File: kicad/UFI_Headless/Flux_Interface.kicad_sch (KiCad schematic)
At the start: 55 parts, among them Q10 BSS138DW, Q11 BSS138DW, Q5 2N7002, Q6 BSS138DW, Q7 BSS138DW, Q8 BSS138DW, Q9 BSS138DW, U14 74LVC1G32, U22 TS5A3166DBVR, U30 74LVC2G32, U31 74LVC1G02, U8 74LVC14AD

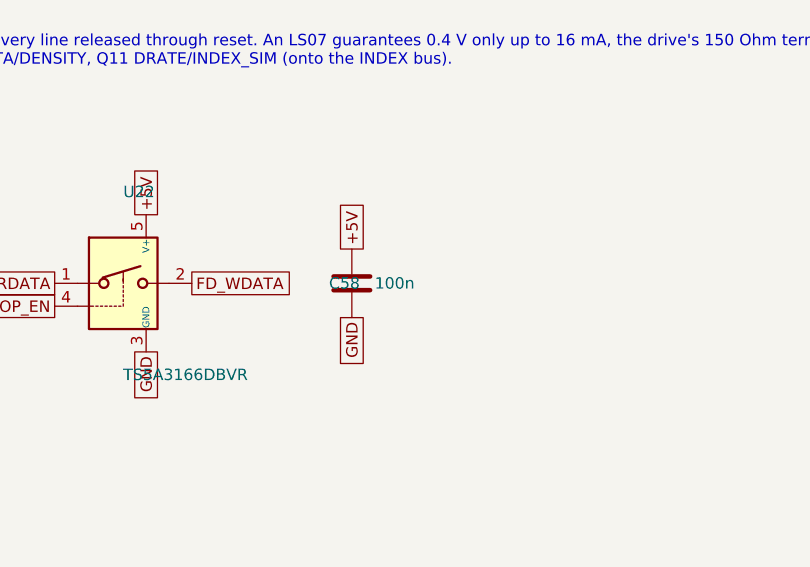
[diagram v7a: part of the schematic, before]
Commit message: KiCad v0.7 rework, stage C part 1 (BOM completion before the release, review note H12): every BOM row now carries an LCSC number, checked against the JLCPCB SMT catalogue on 2026-10-25 (stock in brackets). LAN sheet: U23 W5500 C32843 (9019), J22 HR911105A C12074 (72229, THT), Y2 25 MHz 12 pF +-10 ppm YXC X322525MOB4SI C9006 (basic; load capacitance 12 pF verified on the LCSC parameter page, fits the 18 pF C59/C60), C59/C60 18 pF C0G Yageo CC0603JRNPO9BN180 C107040, C61/C74 10 nF FH 0603B103K500NT C57112 (basic), C71 22 nF Samsung CL10B223KB8NNNC C21122 (basic), C72/C73 6.8 nF FH 0603B682K500NT C1631 (basic), C62 4.7 uF C1779, C63/C69 10 uF C15850, C64-C68/C70 100 nF C14663, FB2 C1002, R109 1M C22935, R111 12.4k 1 % C22865, R112/R113 49.9R 1 % C23185 (basic), R114 10R 1 % C22859 (basic), R115/R116 82R 1 % C23255, R117/R118 330R C23138, R119-R124 10k C25804. Other sheets: R75-R99/R105/R128 1k C21190, R74/R107/R108 10k C25804, R101-R104/R130 470R C23179, R106/R131 100k C25803, C58 100 nF C14663 (value text 100n -> 100nF so it groups with the other 100 nF), D18-D26/D28/D29 PESD3V3L1BA C51450 (48710) like D32-D34, Q5 2N7002 C8545 (basic), U22 TS5A3166DBVR C353035 (10678), J2 DC-005 2.0 C16214 (92305; same pin pattern as the KiCad BarrelJack_Horizontal footprint, placement to be checked in the JLC viewer), J7 2x12 IDC ZHOURI DC3-2.54-24PAS C5144580 (stock 81 - hand soldering stays the recommendation in docs/Bestellung_JLC.md), J12 2x8 IDC DC3-2.54-16PAS C2977594 (4335), J16 2x5 pin header XFCN PZ254V-12-10P C492422 (105667), J21 2x10 pin header PZ254V-12-20P C492427 (63622). Solder jumpers JP5-JP8 are excluded from the BOM (in_bom no) like JP1/JP3 - bare copper, nothing to place. Stock of the review's watch list: U9 SN74LS07DR C371970 4776, D31 ESDA6V1-5SC6 C6650 3010, L1 SRN6045TA-150M C1330797 1866. BOM export (kicad-cli sch export bom, grouped by value/footprint/LCSC): 99 rows, 0 without LCSC, 0 DNP. ERC over the whole project 0 errors / 0 warnings (build/erc.rpt). No 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
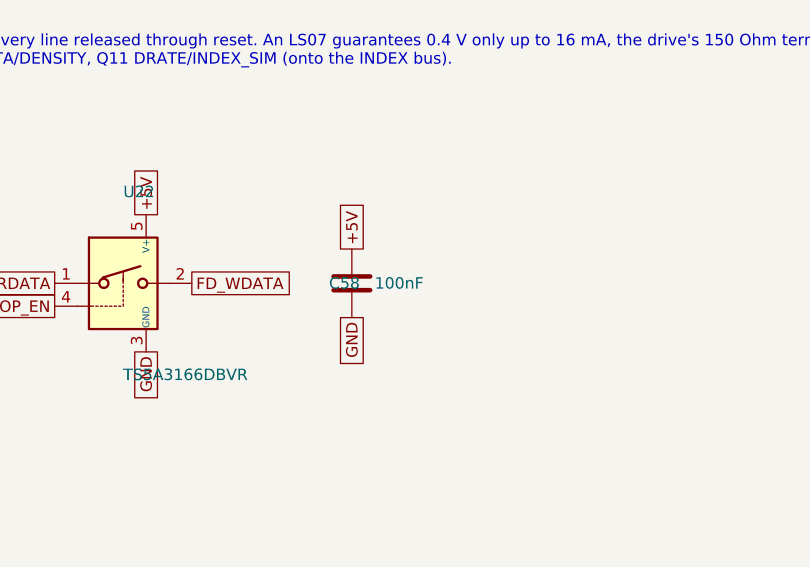
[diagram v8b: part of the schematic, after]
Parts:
- C58: value 100n -> 100nF; LCSC (none) -> C14663
- Q5: LCSC (none) -> C8545
- R106, R131: LCSC (none) -> C25803
- R75, R76, R77, R78, R79, R80, R81, R82, R83, R84, R85, R86, R87, R88, R89, R90, R91: LCSC (none) -> C21190
- U22: LCSC (none) -> C353035
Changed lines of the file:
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@@
+			)
+		)
+		(property "LCSC" "C21190"
+			(at 163.322 250.19 90)
+			(effects
+				(font
+					(size 1.27 1.27)
+				)
+				(hide yes)
 			)
 		)
@@
 			)
 		)
+		(property "LCSC" "C21190"
+			(at 165.862 250.19 90)
+			(effects
+				(font
+					(size 1.27 1.27)
+				)
+				(hide yes)
+			)
+		)
 		(property "Footprint" "Resistor_SMD:R_0603_1608Metric"
 			(at 165.862 250.19 90)
@@
 			)
 		)
+		(property "LCSC" "C21190"
+			(at 168.402 250.19 90)
+			(effects
+				(font
+					(size 1.27 1.27)
+				)
+				(hide yes)
+			)
+		)
 		(property "Footprint" "Resistor_SMD:R_0603_1608Metric"
 			(at 168.402 250.19 90)
@@
 			)
 		)
+		(property "LCSC" "C21190"
+			(at 170.942 250.19 90)
+			(effects
+				(font
+					(size 1.27 1.27)
+				)
+				(hide yes)
+			)
+		)
 		(property "Footprint" "Resistor_SMD:R_0603_1608Metric"
 			(at 170.942 250.19 90)
@@
 			)
 		)
+		(property "LCSC" "C21190"
+			(at 183.642 250.19 90)
+			(effects
+				(font
+					(size 1.27 1.27)
+				)
+				(hide yes)
+			)
+		)
 		(property "Footprint" "Resistor_SMD:R_0603_1608Metric"
 			(at 183.642 250.19 90)
@@
 			)
 		)
+		(property "LCSC" "C21190"
+			(at 186.182 250.19 90)
+			(effects
+				(font
+					(size 1.27 1.27)
+				)
+				(hide yes)
+			)
+		)
 		(property "Footprint" "Resistor_SMD:R_0603_1608Metric"
 			(at 186.182 250.19 90)
@@
 			)
 		)
+		(property "LCSC" "C21190"
+			(at 188.722 250.19 90)
+			(effects
+				(font
+					(size 1.27 1.27)
+				)
+				(hide yes)
+			)
+		)
 		(property "Footprint" "Resistor_SMD:R_0603_1608Metric"
 			(at 188.722 250.19 90)
@@
 			)
 		)
+		(property "LCSC" "C21190"
+			(at 191.262 250.19 90)
+			(effects
+				(font
+					(size 1.27 1.27)
+				)
+				(hide yes)
+			)
+		)
 		(property "Footprint" "Resistor_SMD:R_0603_1608Metric"
 			(at 191.262 250.19 90)
@@
 			)
 		)
+		(property "LCSC" "C21190"
+			(at 203.962 250.19 90)
+			(effects
+				(font
+					(size 1.27 1.27)
+				)
+				(hide yes)
+			)
+		)
 		(property "Footprint" "Resistor_SMD:R_0603_1608Metric"
 			(at 203.962 250.19 90)
@@
 			)
 		)
+		(property "LCSC" "C21190"
+			(at 206.502 250.19 90)
+			(effects
+				(font
+					(size 1.27 1.27)
+				)
+				(hide yes)
+			)
+		)
 		(property "Footprint" "Resistor_SMD:R_0603_1608Metric"
 			(at 206.502 250.19 90)
@@
 			)
 		)
+		(property "LCSC" "C21190"
+			(at 209.042 250.19 90)
+			(effects
+				(font
+					(size 1.27 1.27)
+				)
+				(hide yes)
+			)
+		)
 		(property "Footprint" "Resistor_SMD:R_0603_1608Metric"
 			(at 209.042 250.19 90)
@@
 			)
 		)
+		(property "LCSC" "C21190"
+			(at 252.222 171.45 90)
+			(effects
+				(font
+					(size 1.27 1.27)
+				)
+				(hide yes)
+			)
+		)
 		(property "Footprint" "Resistor_SMD:R_0603_1608Metric"
 			(at 252.222 171.45 90)
@@
 			)
 		)
+		(property "LCSC" "C21190"
+			(at 254.762 171.45 90)
+			(effects
+				(font
+					(size 1.27 1.27)
+				)
+				(hide yes)
+			)
+		)
 		(property "Footprint" "Resistor_SMD:R_0603_1608Metric"
 			(at 254.762 171.45 90)
@@
 			)
 		)
+		(property "LCSC" "C21190"
+			(at 257.302 171.45 90)
+			(effects
+				(font
+					(size 1.27 1.27)
+				)
+				(hide yes)
+			)
+		)
 		(property "Footprint" "Resistor_SMD:R_0603_1608Metric"
 			(at 257.302 171.45 90)
@@
 			)
 		)
+		(property "LCSC" "C21190"
+			(at 259.842 171.45 90)
+			(effects
+				(font
+					(size 1.27 1.27)
+				)
+				(hide yes)
+			)
+		)
 		(property "Footprint" "Resistor_SMD:R_0603_1608Metric"
 			(at 259.842 171.45 90)
@@
 			)
 		)
+		(property "LCSC" "C21190"
+			(at 272.542 171.45 90)
+			(effects
+				(font
+					(size 1.27 1.27)
+				)
+				(hide yes)
+			)
+		)
 		(property "Footprint" "Resistor_SMD:R_0603_1608Metric"
 			(at 272.542 171.45 90)
@@
 			)
 		)
+		(property "LCSC" "C21190"
+			(at 275.082 171.45 90)
+			(effects
+				(font
+					(size 1.27 1.27)
+				)
+				(hide yes)
+			)
+		)
 		(property "Footprint" "Resistor_SMD:R_0603_1608Metric"
 			(at 275.082 171.45 90)
@@
 			)
 		)
+		(property "LCSC" "C353035"
+			(at 328.93 250.19 0)
+			(effects
+				(font
+					(size 1.27 1.27)
+				)
+				(hide yes)
+			)
+		)
 		(property "Footprint" "Package_TO_SOT_SMD:SOT-23-5"
 			(at 328.93 250.19 0)
@@
 			)
 		)
-		(property "Value" "100n"
+		(property "Value" "100nF"
 			(at 358.14 254.0 0)
 			(show_name no)
@@
 				)
 				(justify left)
+			)
+		)
+		(property "LCSC" "C14663"
+			(at 356.565 250.19 0)
+			(effects
+				(font
+					(size 1.27 1.27)
+				)
+				(hide yes)
 			)
 		)
@@
 			)
 		)
+		(property "LCSC" "C25803"
+			(at 295.402 271.78 90)
+			(effects
+				(font
+					(size 1.27 1.27)
+				)
+				(hide yes)
+			)
+		)
 		(property "Footprint" "Resistor_SMD:R_0603_1608Metric"
 			(at 295.402 271.78 90)
@@
 				)
 				(justify left)
+			)
+		)
+		(property "LCSC" "C8545"
+			(at 335.28 300.355 0)
+			(effects
+				(font
+					(size 1.27 1.27)
+				)
+				(hide yes)
 			)
 		)
@@
 			)
 		)
+		(property "LCSC" "C25803"
+			(at 92.202 309.88 90)
+			(effects
+				(font
+					(size 1.27 1.27)
+				)
+				(hide yes)
+			)
+		)
